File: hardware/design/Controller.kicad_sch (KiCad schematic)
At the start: 6 parts, among them U401 ATmega32, Y401 16Mhz

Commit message: Editorial change
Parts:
- renumbered C403 to C401, C401 to C402, C402 to C403
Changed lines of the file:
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@@
 		(on_board yes)
 		(dnp no)
-		(property "Reference" "#PWR0404"
+		(property "Reference" "#PWR0406"
 			(at 77.47 134.62 0)
 			(effects
@@
 			(project "VersaLogic_Board_Tester"
 				(path "/ff8d4a26-8d5e-460f-a4b1-dd16f92e80c4/86c8382c-3570-45bc-95ce-4e153d69ad64"
-					(reference "#PWR0404")
+					(reference "#PWR0406")
 					(unit 1)
 				)
@@
 		(on_board yes)
 		(dnp no)
-		(property "Reference" "#PWR0402"
+		(property "Reference" "#PWR0405"
 			(at 40.64 54.61 0)
 			(effects
@@
 			(project "VersaLogic_Board_Tester"
 				(path "/ff8d4a26-8d5e-460f-a4b1-dd16f92e80c4/86c8382c-3570-45bc-95ce-4e153d69ad64"
-					(reference "#PWR0402")
+					(reference "#PWR0405")
 					(unit 1)
 				)
@@
 		(on_board yes)
 		(dnp no)
-		(property "Reference" "C401"
+		(property "Reference" "C402"
 			(at 45.466 35.56 90)
 			(effects
@@
 			(project "VersaLogic_Board_Tester"
 				(path "/ff8d4a26-8d5e-460f-a4b1-dd16f92e80c4/86c8382c-3570-45bc-95ce-4e153d69ad64"
-					(reference "C401")
+					(reference "C402")
 					(unit 1)
 				)
@@
 		(on_board yes)
 		(dnp no)
-		(property "Reference" "#PWR0406"
+		(property "Reference" "#PWR0403"
 			(at 93.98 29.21 0)
 			(effects
@@
 			(project "VersaLogic_Board_Tester"
 				(path "/ff8d4a26-8d5e-460f-a4b1-dd16f92e80c4/86c8382c-3570-45bc-95ce-4e153d69ad64"
-					(reference "#PWR0406")
+					(reference "#PWR0403")
 					(unit 1)
 				)
@@
 		(on_board yes)
 		(dnp no)
-		(property "Reference" "C402"
+		(property "Reference" "C403"
 			(at 45.466 45.72 90)
 			(effects
@@
 			(project "VersaLogic_Board_Tester"
 				(path "/ff8d4a26-8d5e-460f-a4b1-dd16f92e80c4/86c8382c-3570-45bc-95ce-4e153d69ad64"
-					(reference "C402")
+					(reference "C403")
 					(unit 1)
 				)
@@
 		(on_board yes)
 		(dnp no)
-		(property "Reference" "#PWR0401"
+		(property "Reference" "#PWR0404"
 			(at 40.64 44.45 0)
 			(effects
@@
 			(project "VersaLogic_Board_Tester"
 				(path "/ff8d4a26-8d5e-460f-a4b1-dd16f92e80c4/86c8382c-3570-45bc-95ce-4e153d69ad64"
-					(reference "#PWR0401")
+					(reference "#PWR0404")
 					(unit 1)
 				)
@@
 		(on_board yes)
 		(dnp no)
-		(property "Reference" "#PWR0405"
+		(property "Reference" "#PWR0402"
 			(at 80.01 22.86 0)
 			(effects
@@
 			(project "VersaLogic_Board_Tester"
 				(path "/ff8d4a26-8d5e-460f-a4b1-dd16f92e80c4/86c8382c-3570-45bc-95ce-4e153d69ad64"
-					(reference "#PWR0405")
+					(reference "#PWR0402")
 					(unit 1)
 				)
@@
 		(on_board yes)
 		(dnp no)
-		(property "Reference" "#PWR0403"
+		(property "Reference" "#PWR0401"
 			(at 53.34 22.86 0)
 			(effects
@@
 			(project "VersaLogic_Board_Tester"
 				(path "/ff8d4a26-8d5e-460f-a4b1-dd16f92e80c4/86c8382c-3570-45bc-95ce-4e153d69ad64"
-					(reference "#PWR0403")
+					(reference "#PWR0401")
 					(unit 1)
 				)
@@
 		(on_board yes)
 		(dnp no)
-		(property "Reference" "C403"
+		(property "Reference" "C401"
 			(at 84.836 20.32 90)
 			(effects
@@
 			(project "VersaLogic_Board_Tester"
 				(path "/ff8d4a26-8d5e-460f-a4b1-dd16f92e80c4/86c8382c-3570-45bc-95ce-4e153d69ad64"
-					(reference "C403")
-					(unit 1)
-				)
+					(reference "C401")
+					(unit 1)
+				)

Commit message: Quality assessment - Changes
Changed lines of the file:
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@@
 	)
 	(hierarchical_label "DIRECTION-SER"
-		(shape input)
+		(shape output)
 		(at 95.25 31.75 0)
 		(effects
@@
 	)
 	(hierarchical_label "SIGNAL-OUT-SER"
-		(shape input)
+		(shape output)
 		(at 95.25 54.61 0)
 		(effects

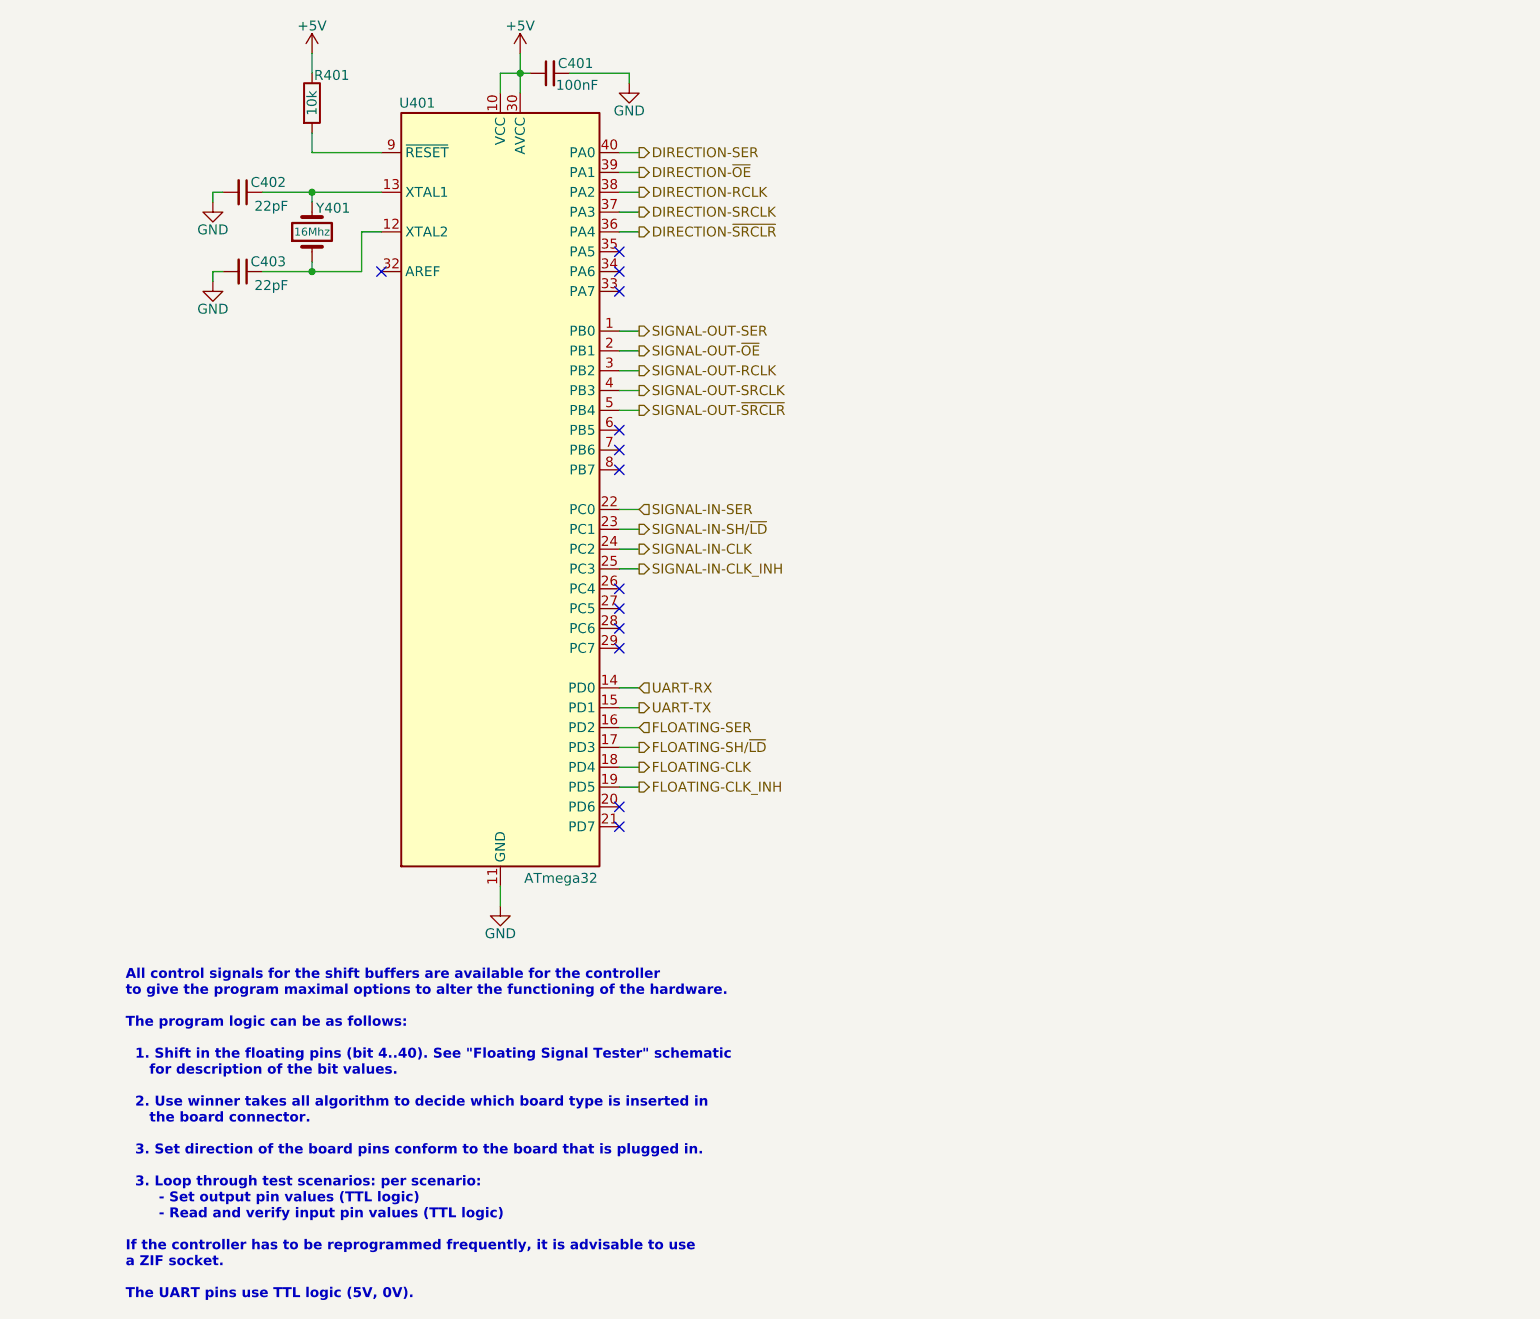
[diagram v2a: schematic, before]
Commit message: Simulating alternative power supply
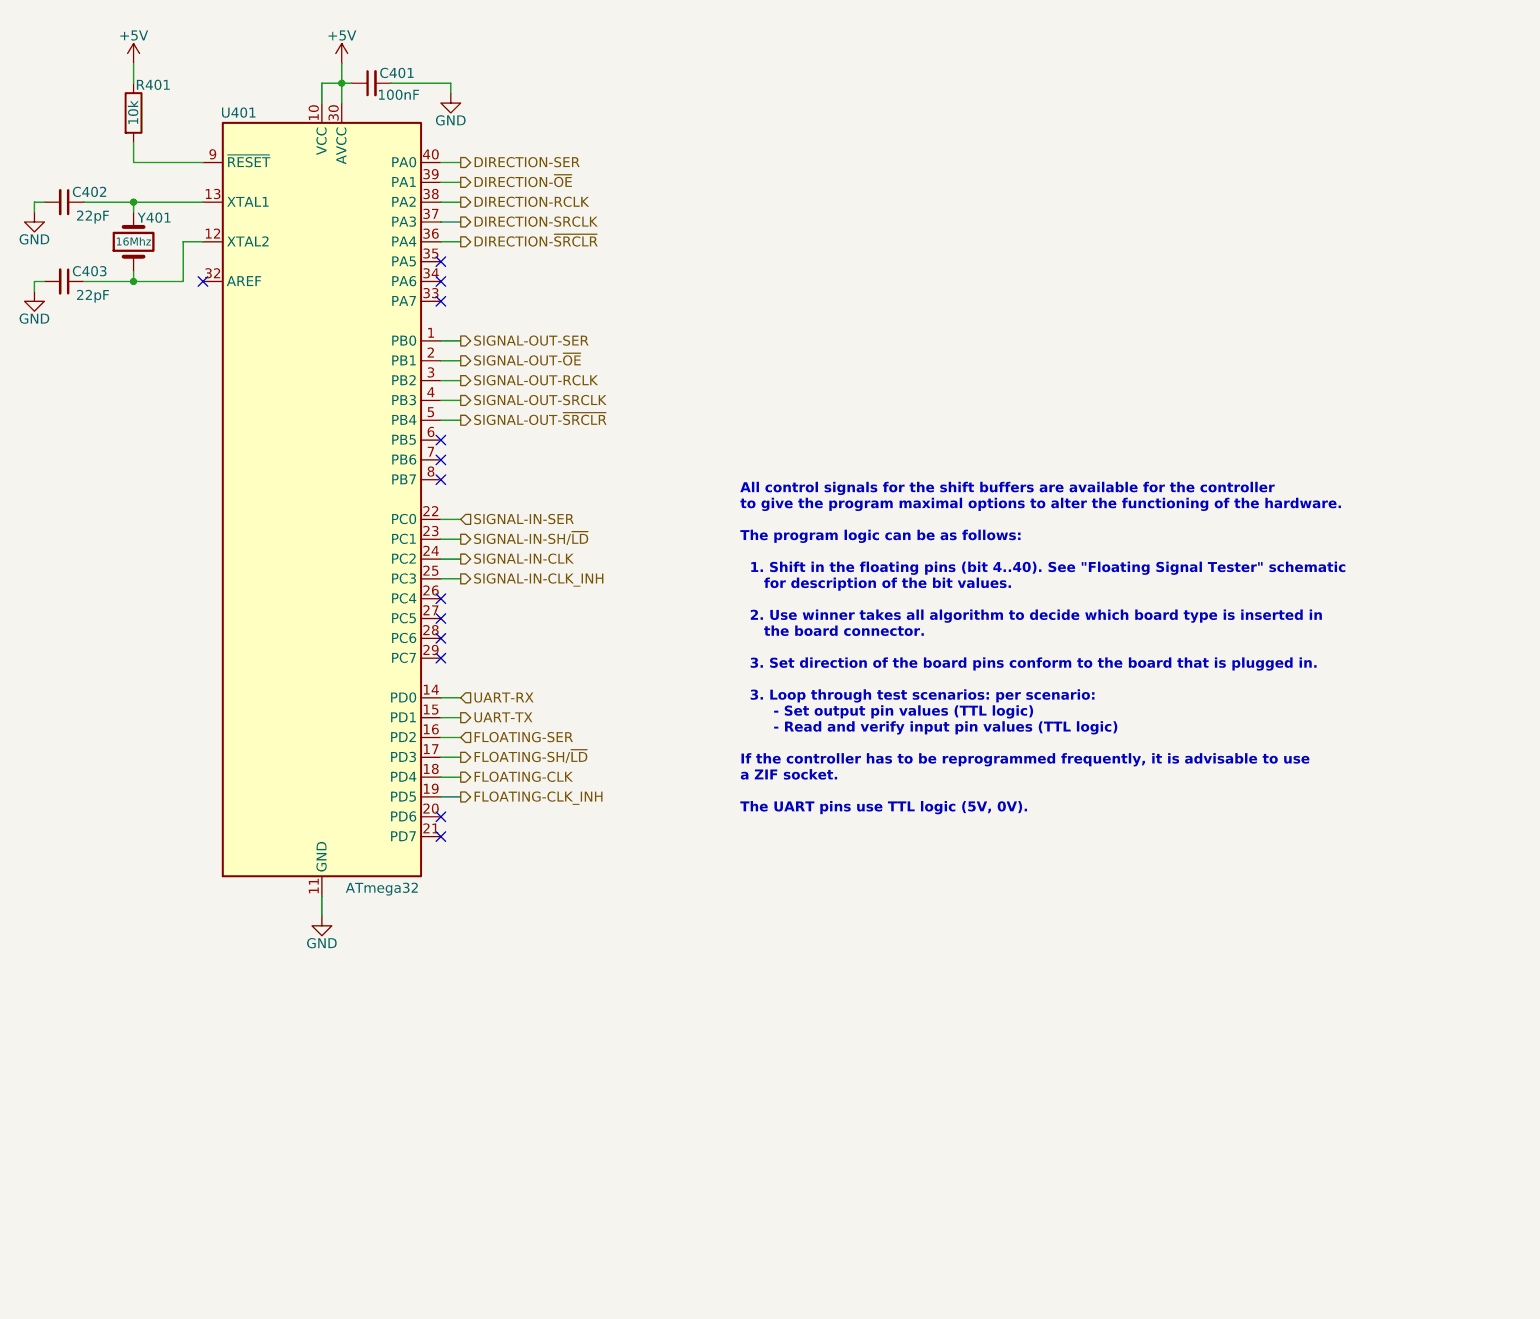
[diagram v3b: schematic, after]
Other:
- moved on the sheet: C401, C402, C403, R401, U401, Y401

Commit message: File cleanup
Added final schematics
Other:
- note added: "All control signals for the shift buffers are available to the controller to give the program maximal options to alter the functioning of the hardware. The program logic can be as follows: 1. Shift in the "floating" pins (bit 4..40). See "Floating Signal Tester" schematic for description of the bit values. 2. Use winner takes all algorithm to decide which board type is inserted in the board conne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"
- note removed: "All control signals for the shift buffers are available for the controller to give the program maximal options to alter the functioning of the hardware. The program logic can be as follows: 1. Shift in the floating pins (bit 4..40). See "Floating Signal Tester" schematic for description of the bit values. 2. Use winner takes all algorithm to decide which board type is inserted in the board connec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"
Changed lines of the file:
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@@
 	(title_block
 		(title "VersaLogic board tester")
-		(date "2025-08-13")
-		(rev "1.0.alpha")
+		(date "2025-09-09")
+		(rev "1.0")
 		(comment 1 "Copyright (c) 2025 by Filip Pynckels & Robin Pynckels")
 	)
-	(text "All control signals for the shift buffers are available for the controller\nto give the program maximal options to alter the functioning of the hardware.\n\nThe program logic can be as follows:\n\n  1. Shift in the floating pins (bit 4..40). See \"Floating Signal Tester\" schematic\n     for description of the bit values.\n\n  2. Use winner takes all algorithm to decide which board type is inserted in\n     the board connector.\n\n  3. Set direction of the board pins conform to the board that is plugged in.\n\n  3. Loop through test scenarios: per scenario:\n       - Set output pin values (TTL logic)\n       - Read and verify input pin values (TTL logic)\n\nIf the controller has to be reprogrammed frequently, it is advisable to use\na ZIF socket.\n\nThe UART pins use TTL logic (5V, 0V)."
+	(text "All control signals for the shift buffers are available to the controller\nto give the program maximal options to alter the functioning of the hardware.\n\nThe program logic can be as follows:\n\n  1. Shift in the \"floating\" pins (bit 4..40). See \"Floating Signal Tester\" schematic\n     for description of the bit values.\n\n  2. Use winner takes all algorithm to decide which board type is inserted in\n     the board connector (on the basis of floating pins and non-floating pins).\n\n  3. Set direction of the board pins conform to the board that is plugged in.\n\n  3. Loop through test scenarios: per scenario:\n       - Set output pin values (TTL logic)\n       - Read and verify input pin values (TTL logic)\n\nIf the controller has to be reprogrammed frequently, it is advisable to use\na ZIF socket.\n\nThe UART pins use TTL logic (5V, 0V)."
 		(exclude_from_sim no)
-		(at 108.204 74.168 0)
+		(at 105.41 74.422 0)
 		(effects
 			(font
